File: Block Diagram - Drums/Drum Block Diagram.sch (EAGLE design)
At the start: 0 parts

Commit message: Changed block diagram
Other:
- note added: "(Dampening)"
- note added: "1+sT"
- note added: "1Vpp"
- note added: "1ms"
- note added: "5V"
- note added: "Bridged-T Oscilator"
- note added: "Buffer + Gain Adjust"
- note added: "Envolope Gen"
- note added: "GAIN"
- note added: "Low Pass Positive Feedback"
- note added: "Negative Feedback"
- note added: "OUT"
- note added: "Ocillator Trigger"
- note added: "TRIG"
- note added: "Trigger"
- note added: "Trigger Buff"
- note added: "VCC = 12V"
- note added: "V_DIODE"

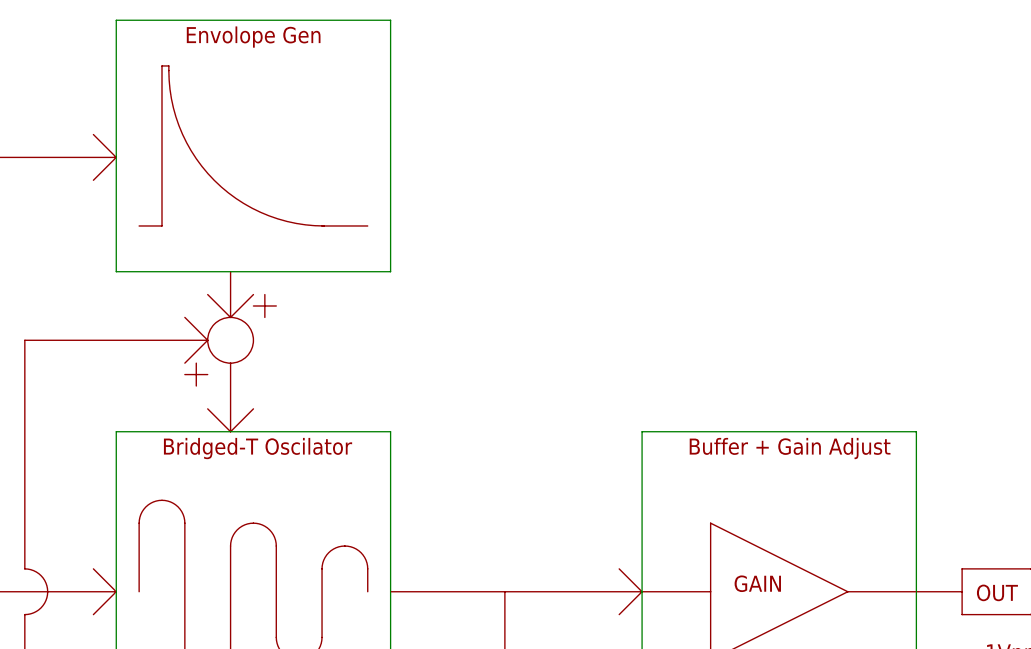
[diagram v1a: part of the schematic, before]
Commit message: updated block diagram
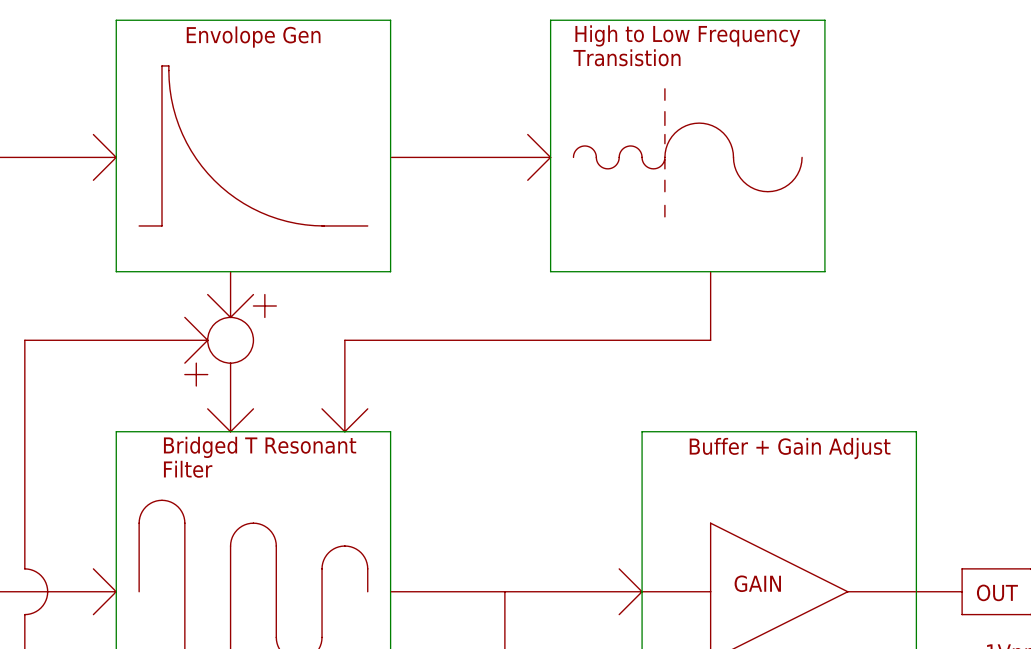
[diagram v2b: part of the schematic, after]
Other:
- note added: "Bridged T Resonant Filter"
- note added: "High to Low Frequency Transistion"
- note removed: "Bridged-T Oscilator"
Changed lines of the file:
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@@
 <wire x1="124.46" y1="101.6" x2="121.92" y2="104.14" width="0.1524" layer="94"/>
 <wire x1="124.46" y1="101.6" x2="121.92" y2="99.06" width="0.1524" layer="94"/>
-<text x="129.54" y="116.84" size="1.778" layer="94">Bridged-T Oscilator</text>
+<text x="129.54" y="114.3" size="1.778" layer="94">Bridged T Resonant
+Filter</text>
 <wire x1="127" y1="101.6" x2="127" y2="109.22" width="0.1524" layer="94"/>
 <wire x1="127" y1="109.22" x2="129.54" y2="111.76" width="0.1524" layer="94" curve="-90"/>
@@
 <text x="220.98" y="93.98" size="1.778" layer="94">1Vpp</text>
 <text x="129.54" y="76.2" size="1.778" layer="94">(Dampening)</text>
+<text x="175.26" y="160.02" size="1.778" layer="94">High to Low Frequency
+Transistion</text>
+<wire x1="154.94" y1="149.86" x2="172.72" y2="149.86" width="0.1524" layer="94"/>
+<wire x1="170.18" y1="152.4" x2="172.72" y2="149.86" width="0.1524" layer="94"/>
+<wire x1="170.18" y1="147.32" x2="172.72" y2="149.86" width="0.1524" layer="94"/>
+<wire x1="190.5" y1="137.16" x2="190.5" y2="129.54" width="0.1524" layer="94"/>
+<wire x1="190.5" y1="129.54" x2="149.86" y2="129.54" width="0.1524" layer="94"/>
+<wire x1="149.86" y1="129.54" x2="149.86" y2="119.38" width="0.1524" layer="94"/>
+<wire x1="152.4" y1="121.92" x2="149.86" y2="119.38" width="0.1524" layer="94"/>
+<wire x1="147.32" y1="121.92" x2="149.86" y2="119.38" width="0.1524" layer="94"/>
+<wire x1="175.26" y1="149.86" x2="177.8" y2="149.86" width="0.1524" layer="94" curve="-180"/>
+<wire x1="177.8" y1="149.86" x2="180.34" y2="149.86" width="0.1524" layer="94" curve="180"/>
+<wire x1="180.34" y1="149.86" x2="182.88" y2="149.86" width="0.1524" layer="94" curve="-180"/>
+<wire x1="182.88" y1="149.86" x2="185.42" y2="149.86" width="0.1524" layer="94" curve="180"/>
+<wire x1="185.42" y1="149.86" x2="193.04" y2="149.86" width="0.1524" layer="94" curve="-180"/>
+<wire x1="193.04" y1="149.86" x2="200.66" y2="149.86" width="0.1524" layer="94" curve="180"/>
+<wire x1="185.42" y1="157.48" x2="185.42" y2="156.21" width="0.1524" layer="94"/>
+<wire x1="185.42" y1="154.94" x2="185.42" y2="153.416" width="0.1524" layer="94"/>
+<wire x1="185.42" y1="152.4" x2="185.42" y2="151.384" width="0.1524" layer="94"/>
+<wire x1="185.42" y1="149.606" x2="185.42" y2="148.59" width="0.1524" layer="94"/>
+<wire x1="185.42" y1="147.32" x2="185.42" y2="146.05" width="0.1524" layer="94"/>
+<wire x1="185.42" y1="144.526" x2="185.42" y2="143.256" width="0.1524" layer="94"/>
 </plain>
 <instances>
@@
 <wire x1="124.46" y1="137.16" x2="124.46" y2="165.1" width="0.1524" layer="91"/>
 </segment>
+<segment>
+<wire x1="172.72" y1="165.1" x2="203.2" y2="165.1" width="0.1524" layer="91"/>
+<wire x1="203.2" y1="165.1" x2="203.2" y2="137.16" width="0.1524" layer="91"/>
+<wire x1="203.2" y1="137.16" x2="172.72" y2="137.16" width="0.1524" layer="91"/>
+<wire x1="172.72" y1="137.16" x2="172.72" y2="165.1" width="0.1524" layer="91"/>
+</segment>
 </net>
